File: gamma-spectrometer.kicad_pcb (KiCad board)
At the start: 2 copper layers, 140.3 x 36.5 mm, 51 parts, among them Q3 MMBT5088LT1G, Q4 MMBT5088LT1G, T1 T1-1T-KK81, U1 Pico 2, U2 MAX1422ECM+D, U3 TLV3201AIDBVR, U4 MAX5026EUT_T, U5 TPS7B6950DBVR, U6 MICROFC-60035-SMT-TR1

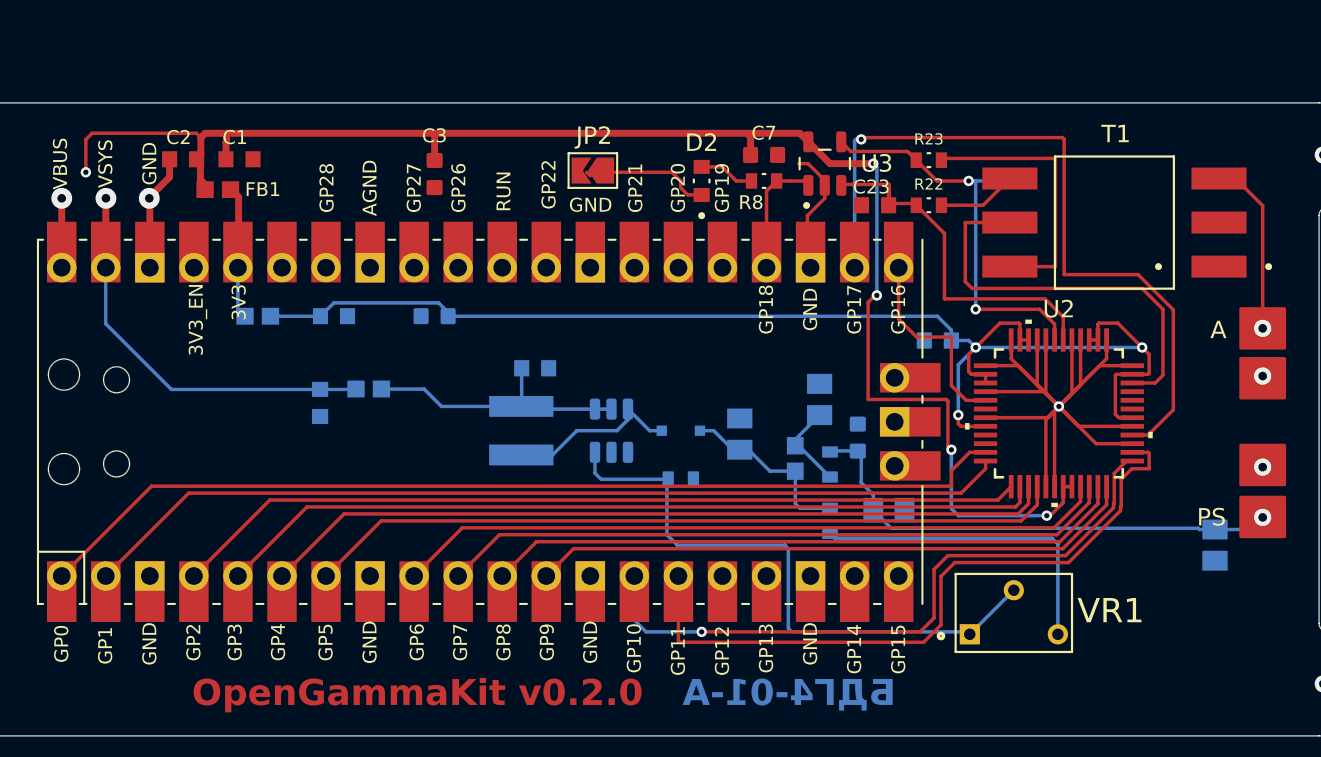
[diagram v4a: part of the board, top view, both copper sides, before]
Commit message: MCP41050 replaces pot for SiPM PS regulation
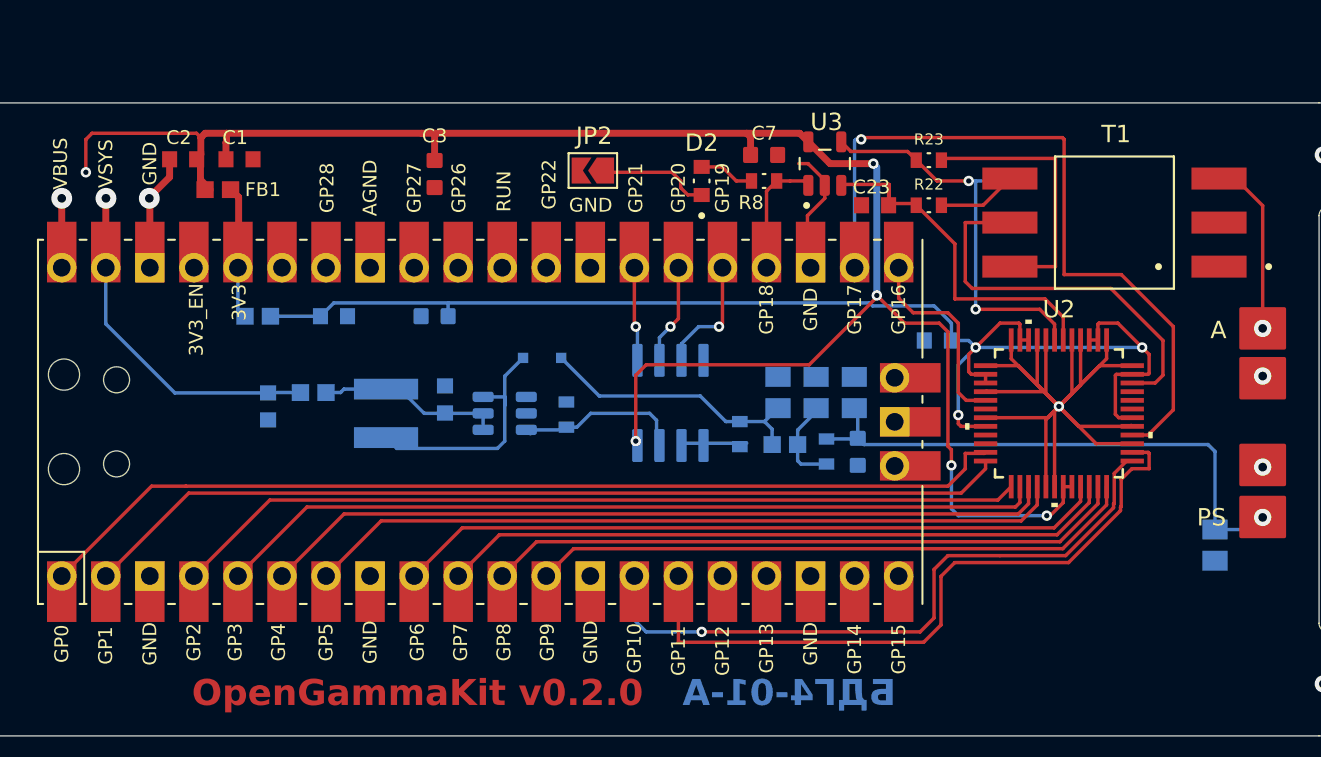
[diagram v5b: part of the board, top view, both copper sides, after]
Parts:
- removed VR1: 50k, 3266W-1-503:TRIM_3266W-1-503
- added U6: MCP41050-I_SN, MCP41050-I_SN:SOIC127P600X175-8N, B.Cu at (124.6, 82.8)
- moved D5 9.04 mm to (117.2, 80.2)
- moved L1 7.86 mm to (108.2, 83.4)
- moved R14 7.58 mm to (118.6, 83.5), turned to -90 degrees
- moved R15 7.21 mm to (128.6, 84.6)
- moved C14 7.09 mm to (135.2, 82.2), turned to 90 degrees
- moved U4 6.24 mm to (115.0, 83.4), turned to 180 degrees
- moved C11 5.50 mm to (111.6, 82.6), turned to 90 degrees
- moved C12 3.26 mm to (130.8, 82.2)
- moved FB3 3.21 mm to (104.0, 82.2)
- moved C18 3.01 mm to (101.4, 83.0)
- moved FB2 1.00 mm to (131.2, 85.2), turned to 180 degrees
- moved C16 0.82 mm to (135.4, 85.6), turned to 90 degrees
- moved R16 0.78 mm to (133.6, 85.6)
- moved C13 0.45 mm to (133.0, 82.2)
- renumbered U6 to U7
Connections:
- U1 pad 25: unconnected-(U1-GPIO19-Pad25)_1 -> SI
- U1 pad 26: unconnected-(U1-GPIO20-Pad26)_1 -> SCK
- U1 pad 27: unconnected-(U1-GPIO21-Pad27) -> CS
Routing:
- net Net-(U4-FB): track 34.8 -> 10.1 mm
- net VCC: track 89.2 -> 107.0 mm, vias 5 -> 6
- net Net-(U6-PA0): track 18.6 -> 3.64 mm
- net SI: track 0.00 -> 7.01 mm, vias 0 -> 1
- net SCK: track 0.00 -> 5.80 mm, vias 0 -> 1
- net CS: track 0.00 -> 5.42 mm, vias 0 -> 1
- net Net-(D5-K): track 10.4 -> 15.9 mm
- net Vdrive: track 16.0 -> 10.6 mm
- net Net-(D5-A): track 10.1 -> 14.3 mm
- net PS_OUT: track 29.3 -> 32.7 mm
- net +5V: track 23.4 -> 20.3 mm
- net CML: track 23.8 -> 22.7 mm
- net AVDD: track 77.6 -> 78.7 mm
- net Net-(C13-Pad1): track 5.33 -> 6.29 mm
- net /PD: track 43.0 -> 42.5 mm

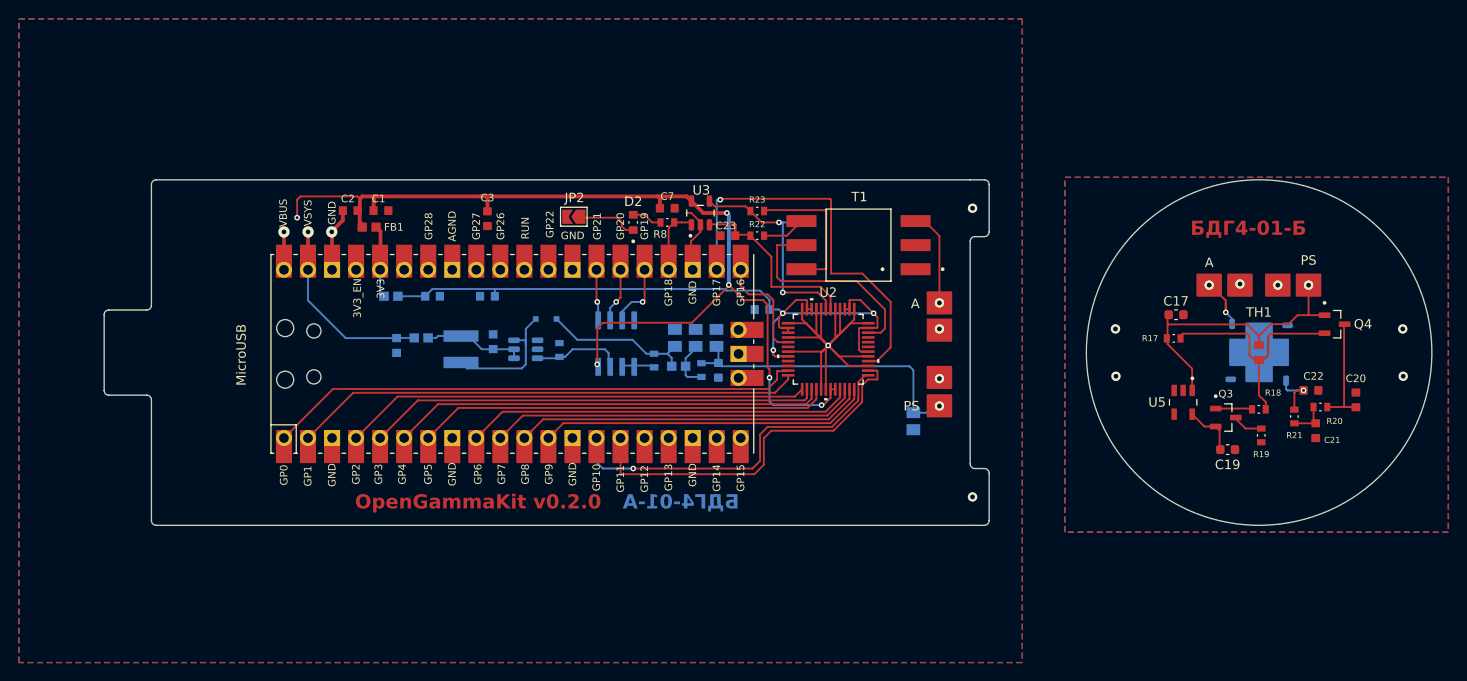
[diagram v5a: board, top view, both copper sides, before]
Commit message: ADC capacitors
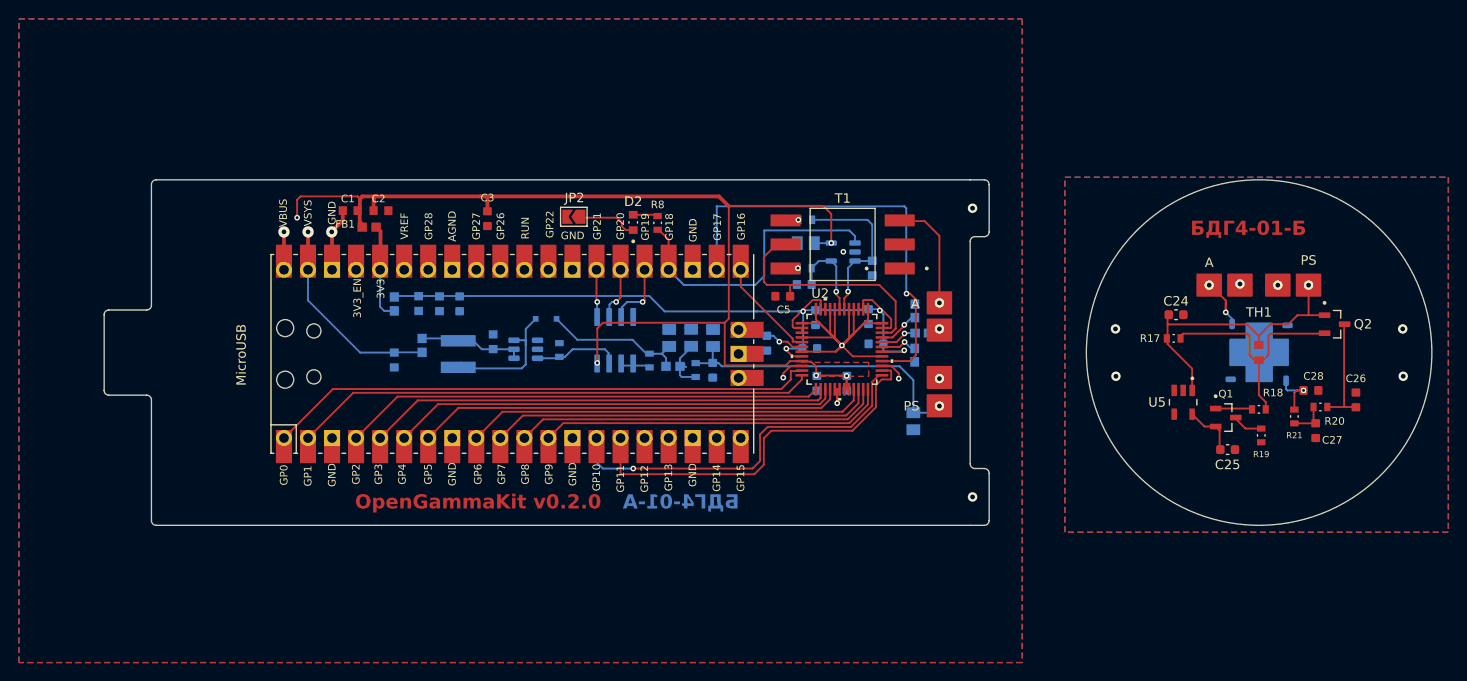
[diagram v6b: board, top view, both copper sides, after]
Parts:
- added C11: 100n, CL10B104KC8NNNC:CAPC1608X90N, B.Cu at (140.5, 82.8)
- added C12: 100n, CL10B104KC8NNNC:CAPC1608X90N, B.Cu at (145.8, 87.0)
- added C13: 100n, CL10B104KC8NNNC:CAPC1608X90N, B.Cu at (145.1, 83.3)
- added C22: 4.7u, CL21A475KBQNNNE:CAPC2012X140N, B.Cu at (144.6, 72.2)
- added C29: 100n, CL10B104KC8NNNC:CAPC1608X90N, B.Cu at (149.0, 87.0)
- added C30: 0.22uF, C1608JB1H224K080AB:CAPC1608X90N, B.Cu at (156.1, 84.0)
- added C31: 0.22uF, C1608JB1H224K080AB:CAPC1608X90N, B.Cu at (156.9, 81.7)
- added C32: 0.22uF, C1608JB1H224K080AB:CAPC1608X90N, B.Cu at (156.2, 79.3)
- added C4: 100n, CL10B104KC8NNNC:CAPC1608X90N, B.Cu at (151.2, 80.0)
- added C5: 100n, CL10B104KC8NNNC:CAPC1608X90N, F.Cu at (142.2, 77.8)
- added C6: 100n, CL10B104KC8NNNC:CAPC1608X90N, B.Cu at (152.0, 82.8)
- C20: renamed from C23; moved to B.Cu
- C7, R22, R23, U3: moved to B.Cu
- moved C8 36.3 mm to (103.7, 78.6), turned to -90 degrees
- moved C7 19.5 mm to (145.6, 80.1), turned to 90 degrees
- moved C20 15.6 mm to (151.7, 74.8), turned to 90 degrees
- moved U3 15.6 mm to (148.6, 73.1), turned to 180 degrees
- moved R23 7.85 mm to (144.5, 74.8), turned to 0 degrees
- moved C21 6.56 mm to (144.5, 76.6), turned to 0 degrees
- moved R22 5.35 mm to (144.6, 69.7), turned to 0 degrees
- moved C10 3.05 mm to (108.1, 78.6), turned to 90 degrees
- moved T1 1.68 mm to (148.5, 72.3)
- moved C19 1.55 mm to (101.2, 84.5)
- moved U2 1.45 mm to (148.4, 83.4)
- moved C9 1.08 mm to (105.9, 78.6), turned to -90 degrees
- moved R8 1.02 mm to (129.0, 70.0), turned to -90 degrees
- moved FB4 0.89 mm to (101.2, 78.6), turned to 90 degrees
- moved FB3 0.80 mm to (104.1, 83.0), turned to -90 degrees
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- renumbered C2 to C1, C16 to C14, C14 to C16, C13 to C17, C12 to C18, C18 to C19, C1 to C2, C24 to C21, C11 to C23, C17 to C24, C19 to C25, C20 to C26, C21 to C27, C22 to C28, D5 to D1, Q3 to Q1, Q4 to Q2
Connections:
- C7 pad 2: VCC -> AVDD
- U2 pad 18: unconnected-(U2-*CLK-Pad18) -> Net-(U2-*CLK)
- U2 pad 21: unconnected-(U2-DVDD-Pad21) -> VCC
- U2 pad 22: unconnected-(U2-DGND-Pad22) -> GND
- U2 pad 43: unconnected-(U2-REFIN-Pad43) -> Net-(U2-REFIN)
- U2 pad 44: unconnected-(U2-REFP-Pad44) -> Net-(U2-REFP)
- U2 pad 45: unconnected-(U2-REFN-Pad45) -> Net-(U2-REFN)
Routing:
- net INT: track 11.3 -> 31.4 mm
- net GND: track 85.7 -> 70.6 mm, vias 6 -> 10
- net VCC: track 107.0 -> 121.4 mm, vias 6 -> 5
- net Net-(R23-Pad1): track 15.5 -> 1.32 mm, vias 0 -> 1
- net INN: track 23.1 -> 9.63 mm, vias 2 -> 1
- net AVDD: track 78.7 -> 85.4 mm, vias 3 -> 4
- net Net-(R22-Pad1): track 4.73 -> 0.00 mm, vias 0 -> 1
- net Net-(U2-REFN): track 0.00 -> 4.39 mm, vias 0 -> 1
- net /PD: track 42.5 -> 46.8 mm
- net Net-(U2-*CLK): track 0.00 -> 4.26 mm, vias 0 -> 1
- net Net-(U2-REFIN): track 0.00 -> 3.95 mm, vias 0 -> 1
- net Net-(U2-REFP): track 0.00 -> 3.95 mm, vias 0 -> 1
- net CML: track 22.7 -> 26.6 mm
- net INP: track 21.0 -> 18.0 mm, vias 0 -> 1
- net Net-(U1-3V3): track 8.06 -> 10.7 mm
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- added copper zone on F.Cu, net VCC
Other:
- board text added: "GP19"
- board text added: "VREF"

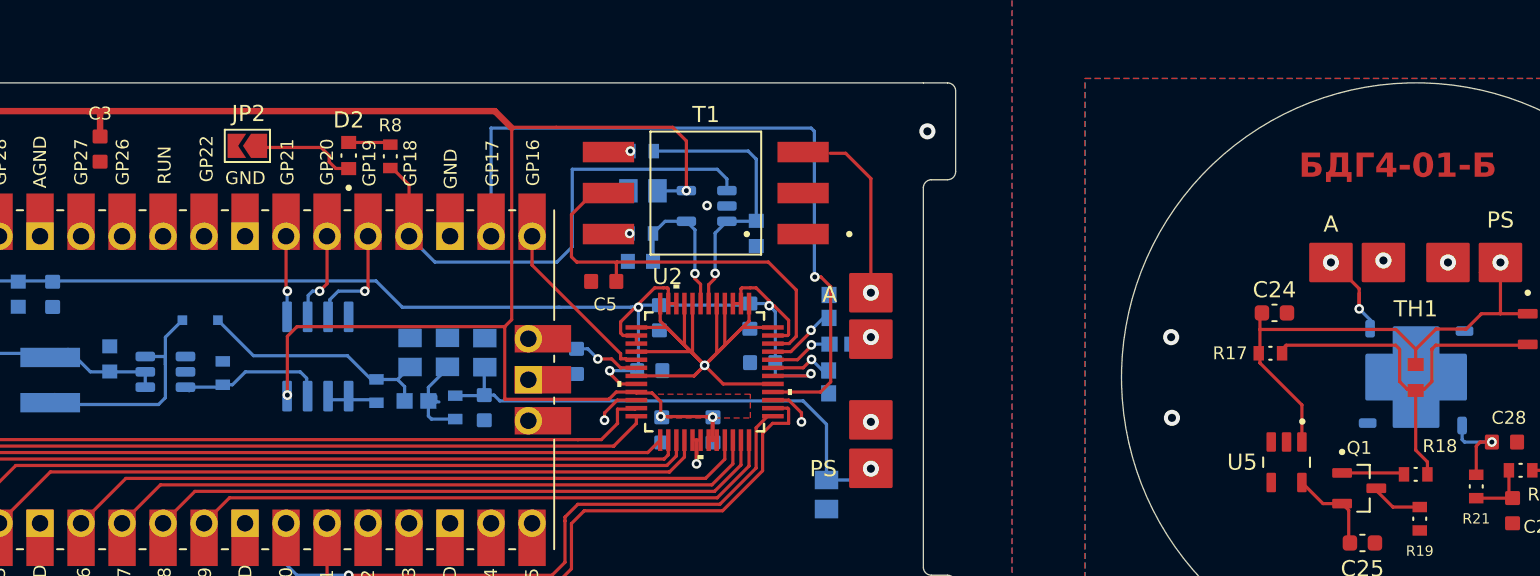
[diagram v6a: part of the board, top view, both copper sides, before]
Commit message: Digital potentiometer improvement
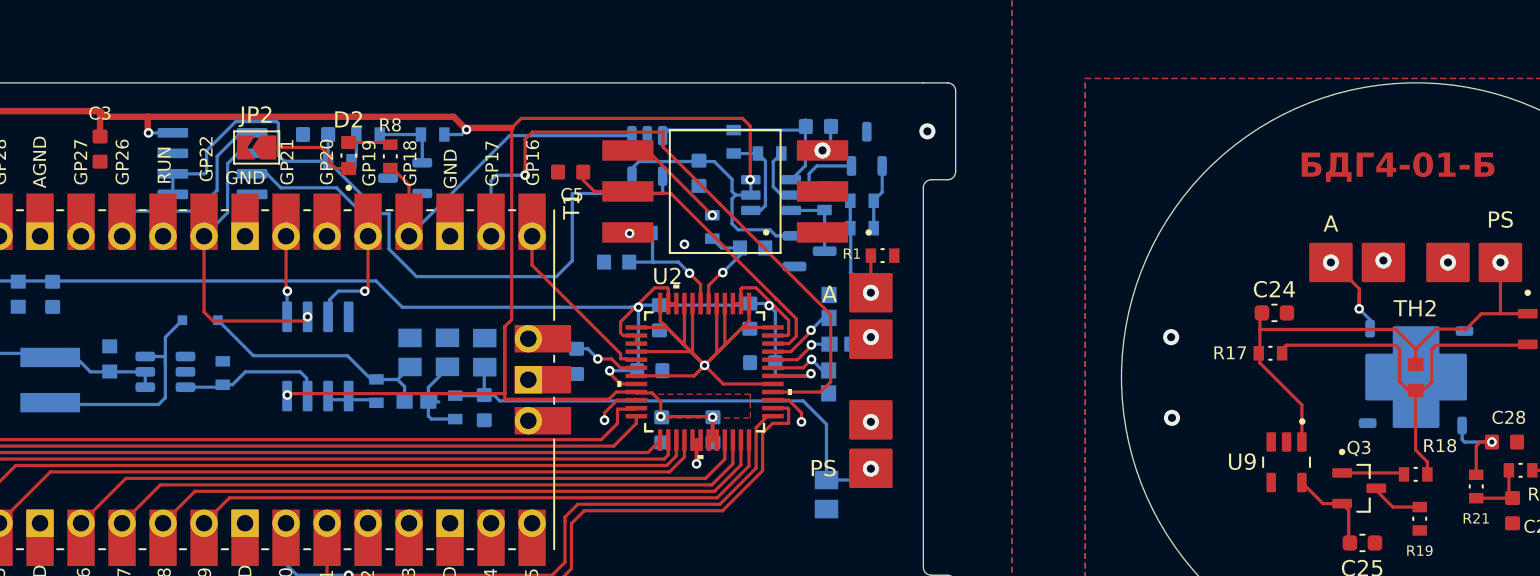
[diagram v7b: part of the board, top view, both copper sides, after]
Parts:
- removed C22: 4.7u, CL21A475KBQNNNE:CAPC2012X140N
- added C33: 100n, CL10B104KC8NNNC:CAPC1608X90N, B.Cu at (155.5, 68.2)
- added C34: 100n, CL10B104KC8NNNC:CAPC1608X90N, B.Cu at (148.1, 71.1)
- added C35: 100n, CL10B104KC8NNNC:CAPC1608X90N, B.Cu at (124.3, 68.7)
- added D3: BAT54S, Package_TO_SOT_SMD:SOT-23, B.Cu at (154.9, 75.9)
- added R1: 1k, ERJ3EKF1001V:RES_ERJ3EKF1001V, F.Cu at (159.5, 76.2)
- added R10: 1k, ERJ3EKF1001V:RES_ERJ3EKF1001V, B.Cu at (131.6, 68.7)
- added R2: 100R, ERJ3EKF1000V:RES_ERJ3EKF1000V, B.Cu at (155.9, 72.7)
- added R3: 1k, ERJ3EKF1001V:RES_ERJ3EKF1001V, B.Cu at (150.2, 69.2)
- added R4: 1k, ERJ3EKF1001V:RES_ERJ3EKF1001V, B.Cu at (152.5, 69.9)
- added R5: 210k, ERJ3EKF2103V:RES_ERJ3EKF2103V, B.Cu at (158.2, 74.5)
- added R6: 210k, ERJ3EKF2103V:RES_ERJ3EKF2103V, B.Cu at (158.2, 72.8)
- added R7: 210k, ERJ3EKF2103V:RES_ERJ3EKF2103V, B.Cu at (125.8, 70.4)
- added R9: 210k, ERJ3EKF2103V:RES_ERJ3EKF2103V, B.Cu at (127.6, 68.7)
- added U11: LM4040AIM3, LM4040AIM3-3_0-T:SOT95P237X112-3N, B.Cu at (129.9, 71.4)
- added U5: LM4040AIM3, LM4040AIM3-3_0-T:SOT95P237X112-3N, B.Cu at (158.5, 69.6)
- added U7: MCP41050-I_SN, MCP41050-I_SN:SOIC127P600X175-8N, B.Cu at (118.0, 70.5)
- added U8: OPA357AIDBVR, OPA357AIDBVR:SOT95P280X145-6N, B.Cu at (152.6, 72.5)
- moved C5 7.08 mm to (140.2, 71.0)
- moved R22 6.40 mm to (148.9, 74.4), turned to -90 degrees
- moved U3 4.81 mm to (144.9, 70.0), turned to -90 degrees
- moved C21 1.48 mm to (143.0, 76.6)
- moved T1 1.21 mm to (149.7, 72.2)
- moved C20 0.93 mm to (151.4, 75.7), turned to 180 degrees
- moved JP2 0.58 mm to (120.7, 69.5)
- renumbered Q1 to Q3, TH1 to TH2, U7 to U10, U5 to U9
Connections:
- net CS renamed CS1
- T1 pad 4: ANODE_IN -> Net-(C33-Pad2)
- U1 pad 26: SCK -> unconnected-(U1-GPIO20-Pad26)_1
- U1 pad 29: unconnected-(U1-GPIO22-Pad29)_1 -> SCK
- U1 pad 31: unconnected-(U1-GPIO26_ADC0-Pad31) -> CS2
- U10 pad 2: unconnected-(U7-Pad2) -> (no net)
- U10 pad 5: unconnected-(U7-EP-Pad5) -> (no net)
- U3 pad 3: INP -> SIG
- U3 pad 4: INN -> Net-(U3-IN-)
- U9 pad 2: unconnected-(U5-NC-Pad2) -> (no net)
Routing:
- net Net-(U3-IN-): track 0.00 -> 47.4 mm
- net VCC: track 121.4 -> 144.5 mm, vias 5 -> 7
- net SIG: track 0.00 -> 13.2 mm
- net CS2: track 0.00 -> 12.8 mm
- net SCK: track 6.01 -> 18.6 mm
- net INP: track 18.0 -> 6.25 mm
- net GND: track 70.6 -> 81.2 mm
- net INT: track 31.4 -> 21.3 mm
- net SI: track 7.29 -> 16.7 mm
- net Net-(R22-Pad1): track 0.00 -> 6.89 mm
- net /PD: track 46.8 -> 40.2 mm
- net Net-(U8--IN): track 0.00 -> 5.95 mm
- net CML: track 26.6 -> 21.1 mm
- net Net-(D3-COM): track 0.00 -> 4.62 mm
- net VREF: track 0.00 -> 4.46 mm
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
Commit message: 3d models update
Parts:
- renumbered TH2 to TH1
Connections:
- U10 pad 2: (no net) -> unconnected-(U10-Pad2)
- U10 pad 5: (no net) -> unconnected-(U10-EP-Pad5)
- U9 pad 2: (no net) -> unconnected-(U9-NC-Pad2)
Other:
- board text added: "OpenGammaKit v0.2.3"
- board text removed: "OpenGammaKit v0.2.0"
